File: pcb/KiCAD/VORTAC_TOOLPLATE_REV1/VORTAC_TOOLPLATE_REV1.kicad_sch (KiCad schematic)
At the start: 10 parts, among them J1 Conn_01x07, J2 Conn_01x02, J3 Conn_01x05

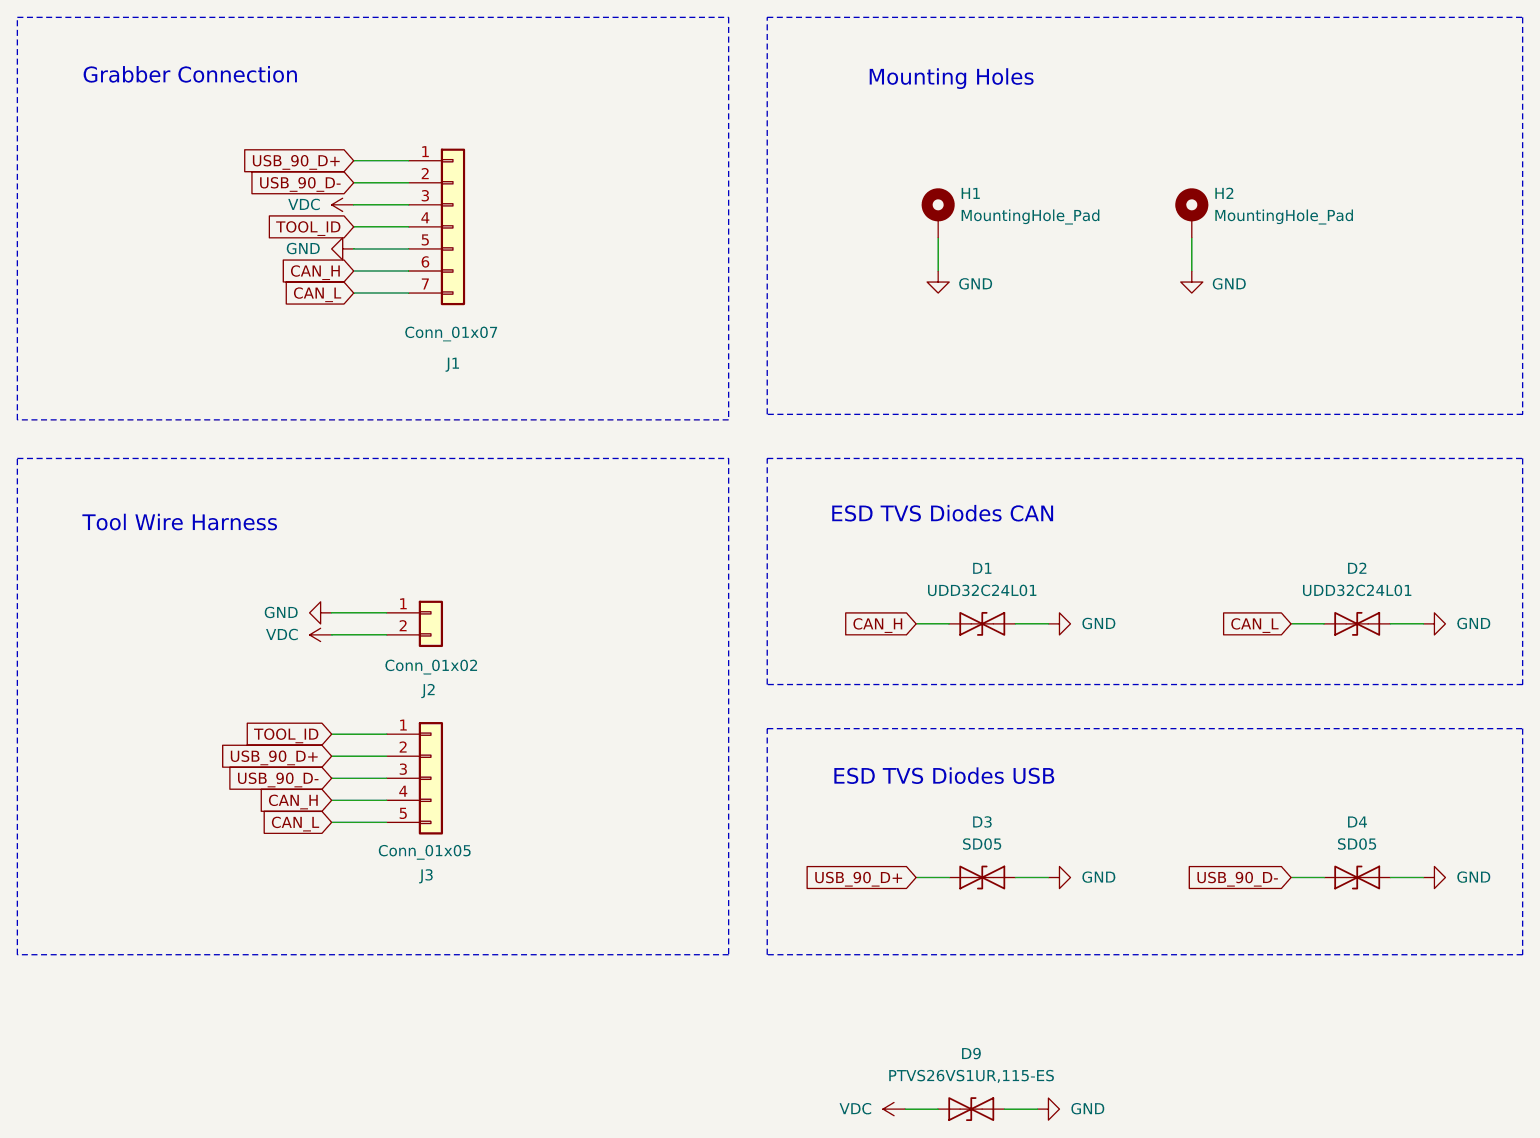
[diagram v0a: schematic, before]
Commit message: Added Dock PCB
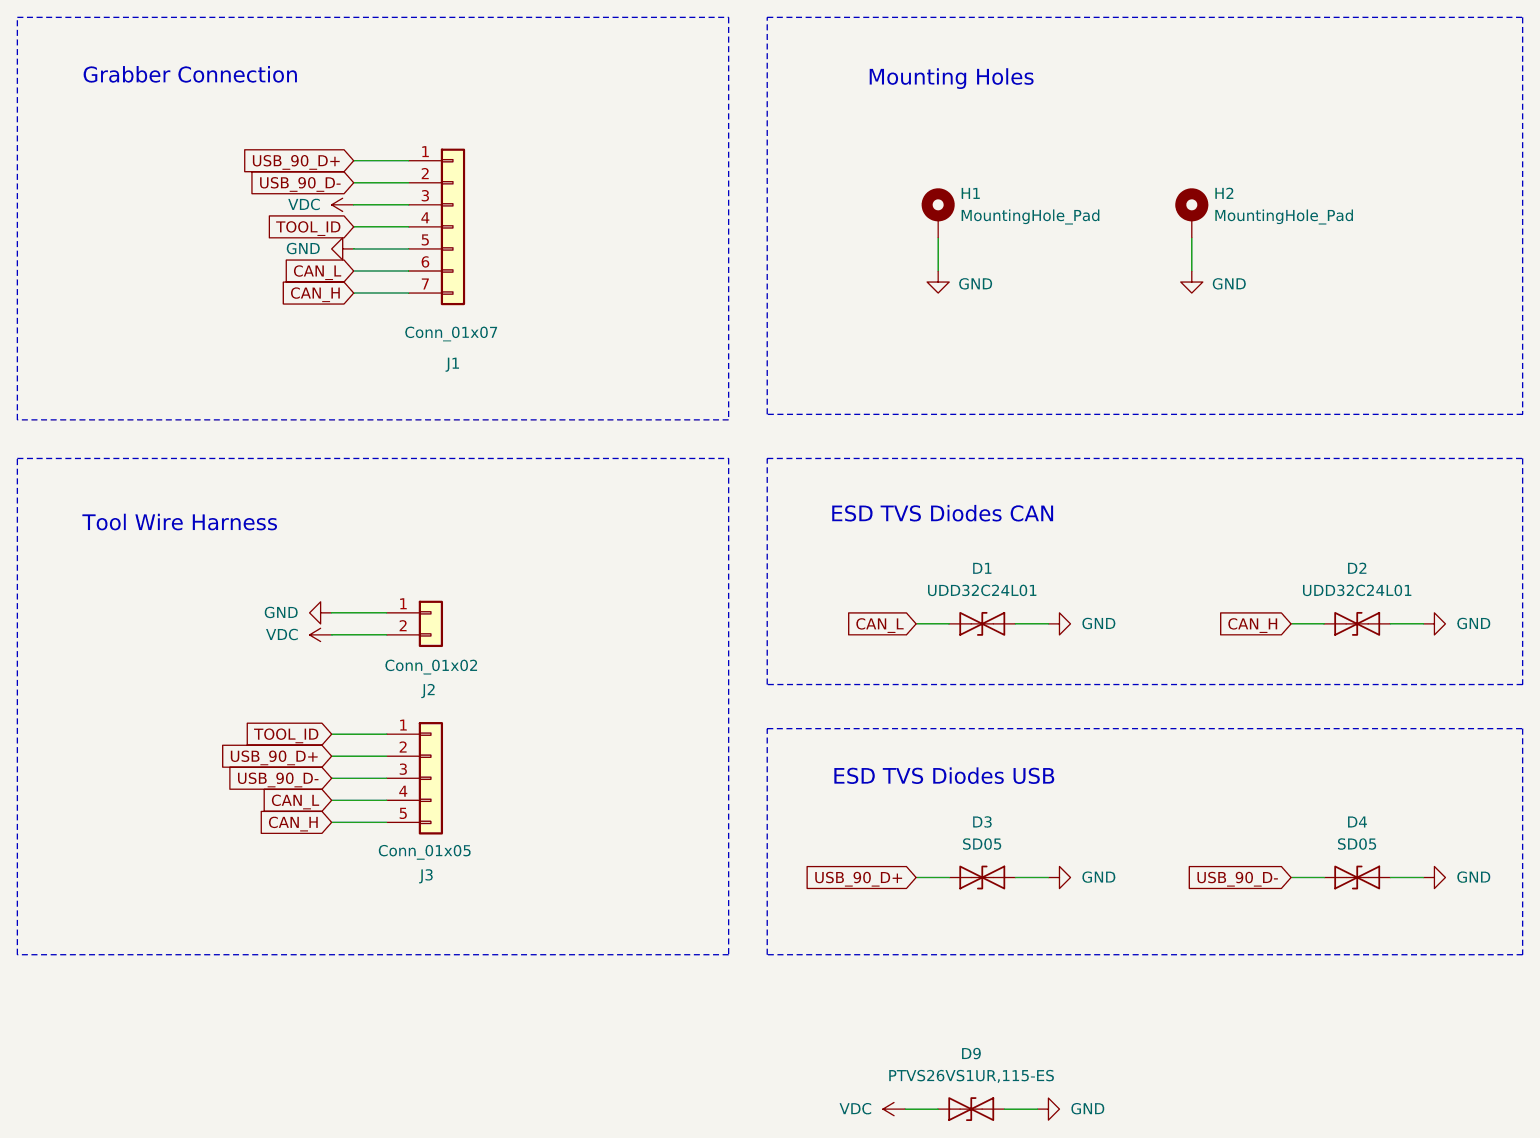
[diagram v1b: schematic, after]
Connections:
- net CAN_H: now also D2.2 (A2), J1.7 (Pin_7), J3.5 (Pin_5); no longer D1.2 (A2), J1.6 (Pin_6), J3.4 (Pin_4)
- net CAN_L: now also D1.2 (A2), J1.6 (Pin_6), J3.4 (Pin_4); no longer D2.2 (A2), J1.7 (Pin_7), J3.5 (Pin_5)
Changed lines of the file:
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@@
 	(global_label "CAN_H"
 		(shape input)
+		(at 166.37 88.9 180)
+		(fields_autoplaced yes)
+		(effects
+			(font
+				(size 1.27 1.27)
+			)
+			(justify right)
+		)
+		(property "Intersheetrefs" "${INTERSHEET_REFS}"
+			(at 157.3976 88.9 0)
+			(effects
+				(font
+					(size 1.27 1.27)
+				)
+				(justify right)
+				(hide yes)
+			)
+		)
+	)
+	(global_label "USB_90_D+"
+		(shape input)
+		(at 58.42 35.56 180)
+		(fields_autoplaced yes)
+		(effects
+			(font
+				(size 1.27 1.27)
+			)
+			(justify right)
+		)
+		(property "Intersheetrefs" "${INTERSHEET_REFS}"
+			(at 44.4282 35.56 0)
+			(effects
+				(font
+					(size 1.27 1.27)
+				)
+				(justify right)
+				(hide yes)
+			)
+		)
+	)
+	(global_label "USB_90_D+"
+		(shape input)
+		(at 123.19 118.11 180)
+		(fields_autoplaced yes)
+		(effects
+			(font
+				(size 1.27 1.27)
+			)
+			(justify right)
+		)
+		(property "Intersheetrefs" "${INTERSHEET_REFS}"
+			(at 109.1982 118.11 0)
+			(effects
+				(font
+					(size 1.27 1.27)
+				)
+				(justify right)
+				(hide yes)
+			)
+		)
+	)
+	(global_label "CAN_H"
+		(shape input)
+		(at 58.42 50.8 180)
+		(fields_autoplaced yes)
+		(effects
+			(font
+				(size 1.27 1.27)
+			)
+			(justify right)
+		)
+		(property "Intersheetrefs" "${INTERSHEET_REFS}"
+			(at 49.4476 50.8 0)
+			(effects
+				(font
+					(size 1.27 1.27)
+				)
+				(justify right)
+				(hide yes)
+			)
+		)
+	)
+	(global_label "USB_90_D+"
+		(shape input)
+		(at 55.88 104.14 180)
+		(fields_autoplaced yes)
+		(effects
+			(font
+				(size 1.27 1.27)
+			)
+			(justify right)
+		)
+		(property "Intersheetrefs" "${INTERSHEET_REFS}"
+			(at 41.8882 104.14 0)
+			(effects
+				(font
+					(size 1.27 1.27)
+				)
+				(justify right)
+				(hide yes)
+			)
+		)
+	)
+	(global_label "CAN_L"
+		(shape input)
 		(at 123.19 88.9 180)
 		(fields_autoplaced yes)
@@
 		)
 		(property "Intersheetrefs" "${INTERSHEET_REFS}"
-			(at 114.2176 88.9 0)
-			(effects
-				(font
-					(size 1.27 1.27)
-				)
-				(justify right)
-				(hide yes)
-			)
-		)
-	)
-	(global_label "USB_90_D+"
-		(shape input)
-		(at 58.42 35.56 180)
-		(fields_autoplaced yes)
-		(effects
-			(font
-				(size 1.27 1.27)
-			)
-			(justify right)
-		)
-		(property "Intersheetrefs" "${INTERSHEET_REFS}"
-			(at 44.4282 35.56 0)
-			(effects
-				(font
-					(size 1.27 1.27)
-				)
-				(justify right)
-				(hide yes)
-			)
-		)
-	)
-	(global_label "USB_90_D+"
-		(shape input)
-		(at 123.19 118.11 180)
-		(fields_autoplaced yes)
-		(effects
-			(font
-				(size 1.27 1.27)
-			)
-			(justify right)
-		)
-		(property "Intersheetrefs" "${INTERSHEET_REFS}"
-			(at 109.1982 118.11 0)
+			(at 114.52 88.9 0)
 			(effects
 				(font
@@
 	(global_label "CAN_H"
 		(shape input)
+		(at 55.88 111.76 180)
+		(fields_autoplaced yes)
+		(effects
+			(font
+				(size 1.27 1.27)
+			)
+			(justify right)
+		)
+		(property "Intersheetrefs" "${INTERSHEET_REFS}"
+			(at 46.9076 111.76 0)
+			(effects
+				(font
+					(size 1.27 1.27)
+				)
+				(justify right)
+				(hide yes)
+			)
+		)
+	)
+	(global_label "TOOL_ID"
+		(shape input)
+		(at 55.88 101.6 180)
+		(fields_autoplaced yes)
+		(effects
+			(font
+				(size 1.27 1.27)
+			)
+			(justify right)
+		)
+		(property "Intersheetrefs" "${INTERSHEET_REFS}"
+			(at 45.3957 101.6 0)
+			(effects
+				(font
+					(size 1.27 1.27)
+				)
+				(justify right)
+				(hide yes)
+			)
+		)
+	)
+	(global_label "USB_90_D-"
+		(shape input)
+		(at 166.37 118.11 180)
+		(fields_autoplaced yes)
+		(effects
+			(font
+				(size 1.27 1.27)
+			)
+			(justify right)
+		)
+		(property "Intersheetrefs" "${INTERSHEET_REFS}"
+			(at 152.3782 118.11 0)
+			(effects
+				(font
+					(size 1.27 1.27)
+				)
+				(justify right)
+				(hide yes)
+			)
+		)
+	)
+	(global_label "CAN_L"
+		(shape input)
 		(at 58.42 48.26 180)
 		(fields_autoplaced yes)
@@
 		)
 		(property "Intersheetrefs" "${INTERSHEET_REFS}"
-			(at 49.4476 48.26 0)
-			(effects
-				(font
-					(size 1.27 1.27)
-				)
-				(justify right)
-				(hide yes)
-			)
-		)
-	)
-	(global_label "USB_90_D+"
-		(shape input)
-		(at 55.88 104.14 180)
-		(fields_autoplaced yes)
-		(effects
-			(font
-				(size 1.27 1.27)
-			)
-			(justify right)
-		)
-		(property "Intersheetrefs" "${INTERSHEET_REFS}"
-			(at 41.8882 104.14 0)
+			(at 49.75 48.26 0)
+			(effects
+				(font
+					(size 1.27 1.27)
+				)
+				(justify right)
+				(hide yes)
+			)
+		)
+	)
+	(global_label "TOOL_ID"
+		(shape input)
+		(at 58.42 43.18 180)
+		(fields_autoplaced yes)
+		(effects
+			(font
+				(size 1.27 1.27)
+			)
+			(justify right)
+		)
+		(property "Intersheetrefs" "${INTERSHEET_REFS}"
+			(at 47.9357 43.18 0)
+			(effects
+				(font
+					(size 1.27 1.27)
+				)
+				(justify right)
+				(hide yes)
+			)
+		)
+	)
+	(global_label "USB_90_D-"
+		(shape input)
+		(at 55.88 106.68 180)
+		(fields_autoplaced yes)
+		(effects
+			(font
+				(size 1.27 1.27)
+			)
+			(justify right)
+		)
+		(property "Intersheetrefs" "${INTERSHEET_REFS}"
+			(at 41.8882 106.68 0)
 			(effects
 				(font
@@
 	(global_label "CAN_L"
 		(shape input)
-		(at 166.37 88.9 180)
-		(fields_autoplaced yes)
-		(effects
-			(font
-				(size 1.27 1.27)
-			)
-			(justify right)
-		)
-		(property "Intersheetrefs" "${INTERSHEET_REFS}"
-			(at 157.7 88.9 0)
-			(effects
-				(font
-					(size 1.27 1.27)
-				)
-				(justify right)
-				(hide yes)
-			)
-		)
-	)
-	(global_label "CAN_H"
-		(shape input)
 		(at 55.88 109.22 180)
 		(fields_autoplaced yes)
@@
 		)
 		(property "Intersheetrefs" "${INTERSHEET_REFS}"
-			(at 46.9076 109.22 0)
-			(effects
-				(font
-					(size 1.27 1.27)
-				)
-				(justify right)
-				(hide yes)
-			)
-		)
-	)
-	(global_label "TOOL_ID"
-		(shape input)
-		(at 55.88 101.6 180)
-		(fields_autoplaced yes)
-		(effects
-			(font
-				(size 1.27 1.27)
-			)
-			(justify right)
-		)
-		(property "Intersheetrefs" "${INTERSHEET_REFS}"
-			(at 45.3957 101.6 0)
-			(effects
-				(font
-					(size 1.27 1.27)
-				)
-				(justify right)
-				(hide yes)
-			)
-		)
-	)
-	(global_label "USB_90_D-"
-		(shape input)
-		(at 166.37 118.11 180)
-		(fields_autoplaced yes)
-		(effects
-			(font
-				(size 1.27 1.27)
-			)
-			(justify right)
-		)
-		(property "Intersheetrefs" "${INTERSHEET_REFS}"
-			(at 152.3782 118.11 0)
-			(effects
-				(font
-					(size 1.27 1.27)
-				)
-				(justify right)
-				(hide yes)
-			)
-		)
-	)
-	(global_label "CAN_L"
-		(shape input)
-		(at 58.42 50.8 180)
-		(fields_autoplaced yes)
-		(effects
-			(font
-				(size 1.27 1.27)
-			)
-			(justify right)
-		)
-		(property "Intersheetrefs" "${INTERSHEET_REFS}"
-			(at 49.75 50.8 0)
-			(effects
-				(font
-					(size 1.27 1.27)
-				)
-				(justify right)
-				(hide yes)
-			)
-		)
-	)
-	(global_label "TOOL_ID"
-		(shape input)
-		(at 58.42 43.18 180)
-		(fields_autoplaced yes)
-		(effects
-			(font
-				(size 1.27 1.27)
-			)
-			(justify right)
-		)
-		(property "Intersheetrefs" "${INTERSHEET_REFS}"
-			(at 47.9357 43.18 0)
-			(effects
-				(font
-					(size 1.27 1.27)
-				)
-				(justify right)
-				(hide yes)
-			)
-		)
-	)
-	(global_label "USB_90_D-"
-		(shape input)
-		(at 55.88 106.68 180)
-		(fields_autoplaced yes)
-		(effects
-			(font
-				(size 1.27 1.27)
-			)
-			(justify right)
-		)
-		(property "Intersheetrefs" "${INTERSHEET_REFS}"
-			(at 41.8882 106.68 0)
-			(effects
-				(font
-					(size 1.27 1.27)
-				)
-				(justify right)
-				(hide yes)
-			)
-		)
-	)
-	(global_label "CAN_L"
-		(shape input)
-		(at 55.88 111.76 180)
-		(fields_autoplaced yes)
-		(effects
-			(font
-				(size 1.27 1.27)
-			)
-			(justify right)
-		)
-		(property "Intersheetrefs" "${INTERSHEET_REFS}"
-			(at 47.21 111.76 0)
-			(effects
-				(font
+			(at 47.21 109.22 0)
+			(effects
+				(font
